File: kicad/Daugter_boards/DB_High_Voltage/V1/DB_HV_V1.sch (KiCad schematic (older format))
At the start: 37 parts, among them P1 CONN_01X19, P2 BNC, P3 CONN_01X19, U1 LM555N

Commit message: updata motor repository for cloning issu
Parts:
- removed P2: BNC, symbol BNC
- added P?: CONN_01X02, symbol CONN_01X02
- added U?: SMA, symbol SMA
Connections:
- wire segments 69 -> 74
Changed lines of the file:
@@
 LIBS:contrib
 LIBS:valves
+LIBS:echopen
+LIBS:DB_HV_V1-cache
 EELAYER 25 0
 EELAYER END
@@
 $EndComp
 Wire Wire Line
-	9250 2850 9250 3200
-Wire Wire Line
-	9250 3200 10850 3200
+	9250 2850 9250 3600
 Connection ~ 9250 2850
-$Comp
-L BNC P2
-U 1 1 57A88B63
-P 10650 3000
-F 0 "P2" H 10660 3120 50  0000 C CNN
-F 1 "BNC" V 10760 2940 50  0000 C CNN
-F 2 "" H 10650 3000 50  0000 C CNN
-F 3 "" H 10650 3000 50  0000 C CNN
-	1    10650 3000
+Wire Wire Line
+	10500 2850 10500 3000
+$Comp
+L SMA U?
+U 1 1 57A862EC
+P 10550 3350
+F 0 "U?" H 10650 3450 60  0000 C CNN
+F 1 "SMA" H 10650 3550 60  0000 C CNN
+F 2 "" H 10550 3350 60  0001 C CNN
+F 3 "" H 10550 3350 60  0001 C CNN
+	1    10550 3350
 	1    0    0    -1
 $EndComp
 Wire Wire Line
-	10500 2850 10500 3000
+	9250 3600 10850 3600
+Wire Wire Line
+	10850 3600 10850 3200
+Connection ~ 10300 3600
+Wire Wire Line
+	10500 3000 9850 3000
+Wire Wire Line
+	9850 3000 9850 3250
+$Comp
+L CONN_01X02 P?
+U 1 1 57A8658A
+P 9550 3300
+F 0 "P?" H 9550 3450 50  0000 C CNN
+F 1 "CONN_01X02" V 9650 3300 50  0000 C CNN
+F 2 "" H 9550 3300 50  0000 C CNN
+F 3 "" H 9550 3300 50  0000 C CNN
+	1    9550 3300
+	-1   0    0    -1
+$EndComp
+Wire Wire Line
+	9750 3350 9750 3600
+Connection ~ 9750 3600
+Wire Wire Line
+	9850 3250 9750 3250
 $EndSCHEMATC

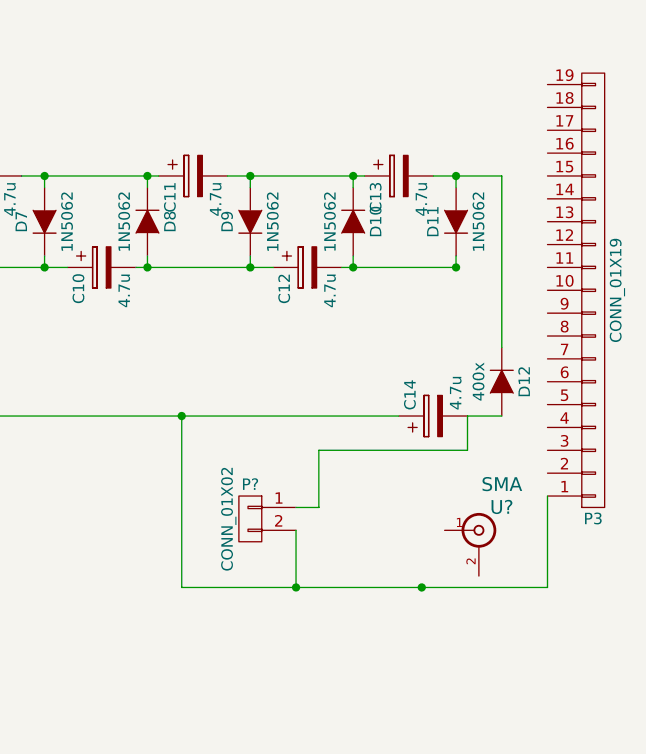
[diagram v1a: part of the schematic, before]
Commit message: adding DB_Filter
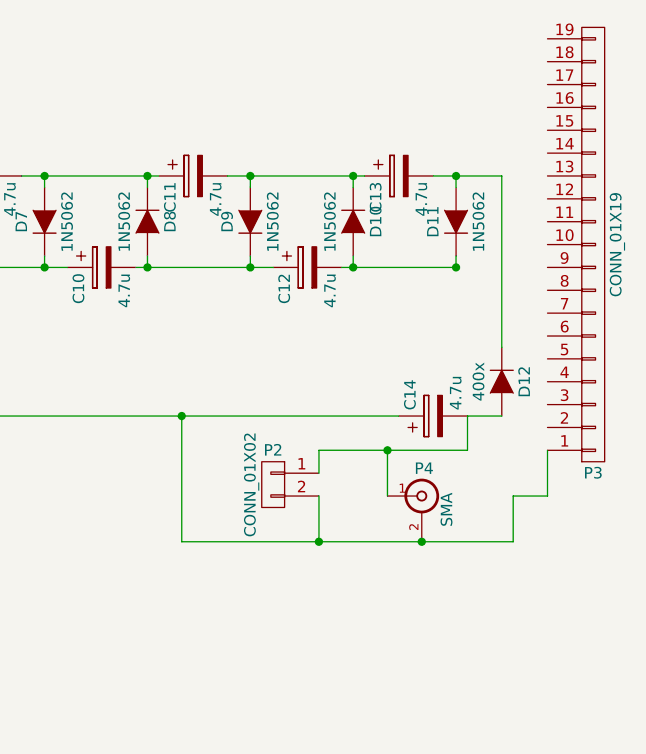
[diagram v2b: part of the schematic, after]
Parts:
- removed U?: SMA, symbol SMA
- added P4: SMA, symbol SMA
- gave numbers to parts that had none: 1
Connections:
- net GND: now also P4.2 (Ext)
- net at C14.2, D12.2 (A), P2.1 (P1): now also P4.1 (In)
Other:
- moved on the sheet: P2, P3
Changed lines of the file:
@@
 EESchema Schematic File Version 2
+LIBS:DB_HV_V1-rescue
 LIBS:power
 LIBS:device
@@
 L CONN_01X19 P3
 U 1 1 57A8893B
-P 11050 2300
-F 0 "P3" H 11050 3300 50  0000 C CNN
-F 1 "CONN_01X19" V 11150 2300 50  0000 C CNN
-F 2 "" H 11050 2300 50  0000 C CNN
-F 3 "" H 11050 2300 50  0000 C CNN
-	1    11050 2300
+P 11050 2100
+F 0 "P3" H 11050 3100 50  0000 C CNN
+F 1 "CONN_01X19" V 11150 2100 50  0000 C CNN
+F 2 "" H 11050 2100 50  0000 C CNN
+F 3 "" H 11050 2100 50  0000 C CNN
+	1    11050 2100
 	1    0    0    1
 $EndComp
 Wire Wire Line
-	9250 2850 9250 3600
+	9250 2850 9250 3400
 Connection ~ 9250 2850
 Wire Wire Line
 	10500 2850 10500 3000
-$Comp
-L SMA U?
-U 1 1 57A862EC
-P 10550 3350
-F 0 "U?" H 10650 3450 60  0000 C CNN
-F 1 "SMA" H 10650 3550 60  0000 C CNN
-F 2 "" H 10550 3350 60  0001 C CNN
-F 3 "" H 10550 3350 60  0001 C CNN
-	1    10550 3350
+Wire Wire Line
+	10500 3000 9850 3000
+$Comp
+L CONN_01X02 P2
+U 1 1 57A8658A
+P 9650 3150
+F 0 "P2" H 9650 3300 50  0000 C CNN
+F 1 "CONN_01X02" V 9750 3150 50  0000 C CNN
+F 2 "" H 9650 3150 50  0000 C CNN
+F 3 "" H 9650 3150 50  0000 C CNN
+	1    9650 3150
+	-1   0    0    -1
+$EndComp
+$Comp
+L SMA P4
+U 1 1 57A88278
+P 10300 3200
+F 0 "P4" H 10310 3320 50  0000 C CNN
+F 1 "SMA" V 10410 3140 50  0000 C CNN
+F 2 "" H 10300 3200 50  0000 C CNN
+F 3 "" H 10300 3200 50  0000 C CNN
+	1    10300 3200
 	1    0    0    -1
 $EndComp
 Wire Wire Line
-	9250 3600 10850 3600
-Wire Wire Line
-	10850 3600 10850 3200
-Connection ~ 10300 3600
-Wire Wire Line
-	10500 3000 9850 3000
-Wire Wire Line
-	9850 3000 9850 3250
-$Comp
-L CONN_01X02 P?
-U 1 1 57A8658A
-P 9550 3300
-F 0 "P?" H 9550 3450 50  0000 C CNN
-F 1 "CONN_01X02" V 9650 3300 50  0000 C CNN
-F 2 "" H 9550 3300 50  0000 C CNN
-F 3 "" H 9550 3300 50  0000 C CNN
-	1    9550 3300
-	-1   0    0    -1
-$EndComp
-Wire Wire Line
-	9750 3350 9750 3600
-Connection ~ 9750 3600
-Wire Wire Line
-	9850 3250 9750 3250
+	9850 3000 9850 3100
+Wire Wire Line
+	10150 3000 10150 3200
+Connection ~ 10150 3000
+Wire Wire Line
+	9250 3400 10700 3400
+Wire Wire Line
+	9850 3200 9850 3400
+Connection ~ 9850 3400
+Wire Wire Line
+	10700 3400 10700 3200
+Wire Wire Line
+	10700 3200 10850 3200
+Connection ~ 10300 3400
+Wire Wire Line
+	10850 3200 10850 3000
 $EndSCHEMATC

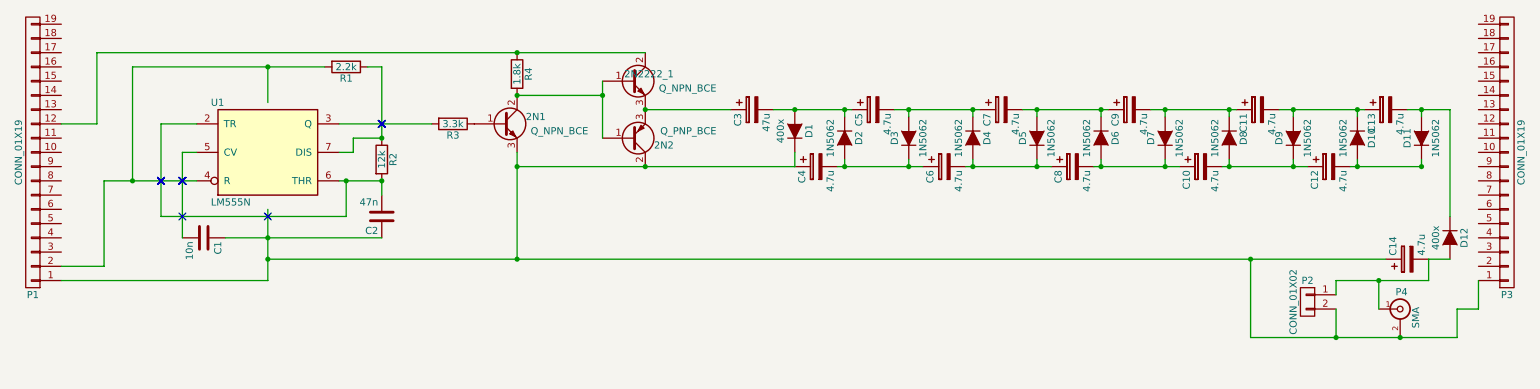
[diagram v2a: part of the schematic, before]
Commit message: adding DB_HV
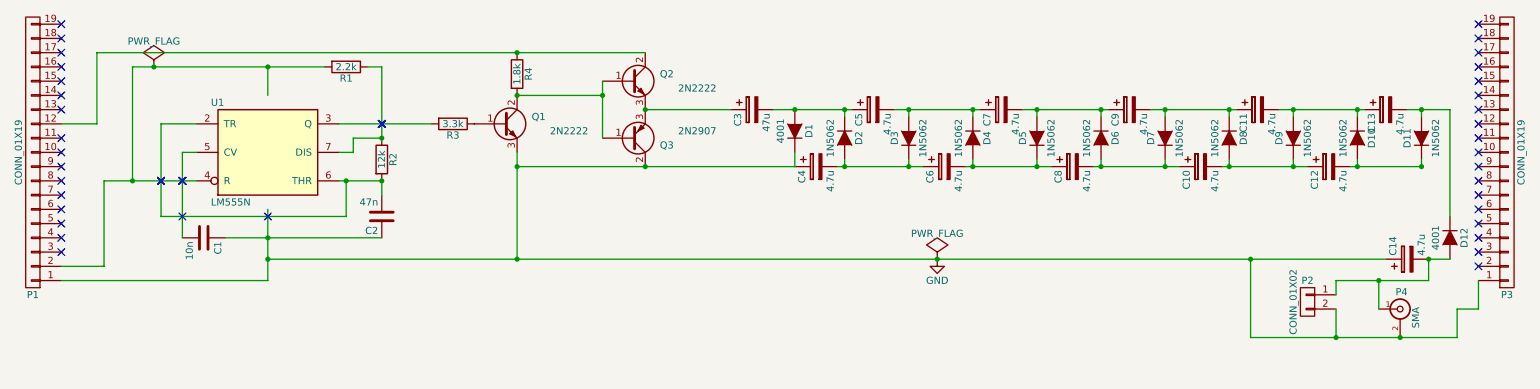
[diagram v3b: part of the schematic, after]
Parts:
- C1, C2: footprint (none) -> Capacitors_ThroughHole:C_Disc_D6_P5
- C10, C11, C12, C13, C14, C3, C4, C5, C6, C7, C8, C9: footprint (none) -> Discret:CP36V
- D1, D12: value 400x -> 4001; footprint (none) -> Diodes_ThroughHole:Diode_DO-35_SOD27_Horizontal_RM10
- D10, D11, D2, D3, D4, D5, D6, D7, D8, D9: footprint (none) -> Diodes_ThroughHole:Diode_DO-35_SOD27_Horizontal_RM10
- P1, P3: footprint (none) -> Socket_Strips:Socket_Strip_Straight_1x19
- P2: footprint (none) -> Socket_Strips:Socket_Strip_Straight_1x02
- P4: footprint (none) -> Connect:bnc
- Q1: renamed from 2N1; value Q_NPN_BCE -> 2N2222; footprint (none) -> Transistors_OldSowjetAera:OldSowjetaera_Transistor_Type-II_BigPads
- Q2: renamed from 2N2222_1; value Q_NPN_BCE -> 2N2222; footprint (none) -> Transistors_OldSowjetAera:OldSowjetaera_Transistor_Type-II_BigPads
- Q3: renamed from 2N2; value Q_PNP_BCE -> 2N2907; footprint (none) -> Transistors_OldSowjetAera:OldSowjetaera_Transistor_Type-II_BigPads
- R1, R2, R3, R4: footprint (none) -> Resistors_ThroughHole:Resistor_Horizontal_RM7mm
- U1: footprint (none) -> Varistors:RV_Disc_D12_W7.1_P7.5
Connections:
- net VCC: now also P1.2 (P2), R1.2, U1.4 (R)
- no-connect marks 14 -> 48
